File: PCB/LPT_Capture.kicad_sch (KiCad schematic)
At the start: 13 parts, among them J1 USB3155-30-A, J2 DB25P064TXLF, U1 FT245RL

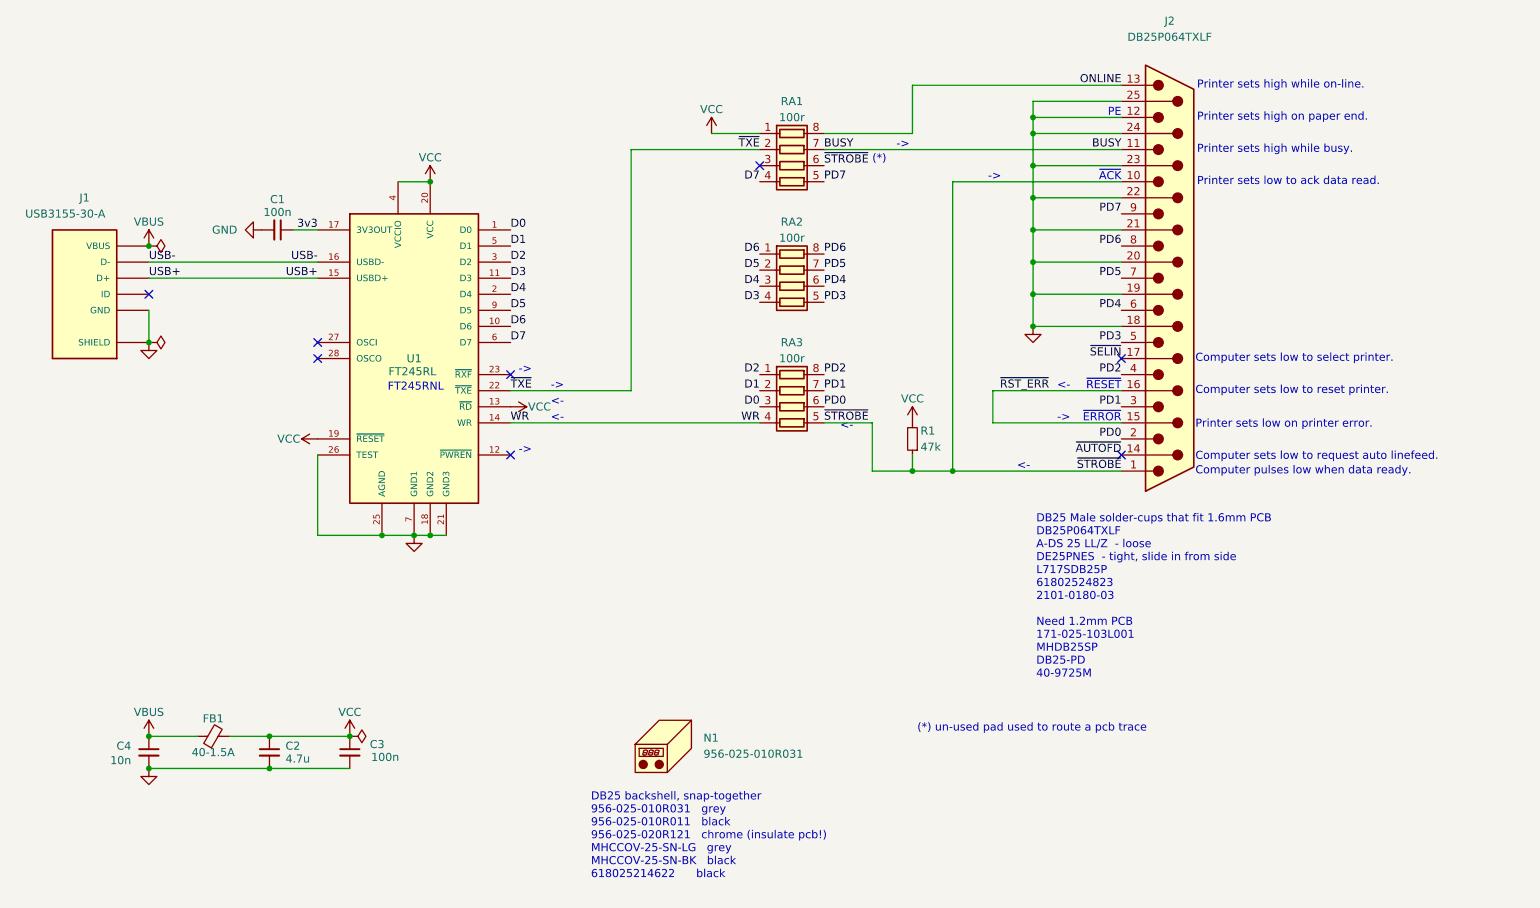
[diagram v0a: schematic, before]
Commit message: strobe>ack via unused 100r
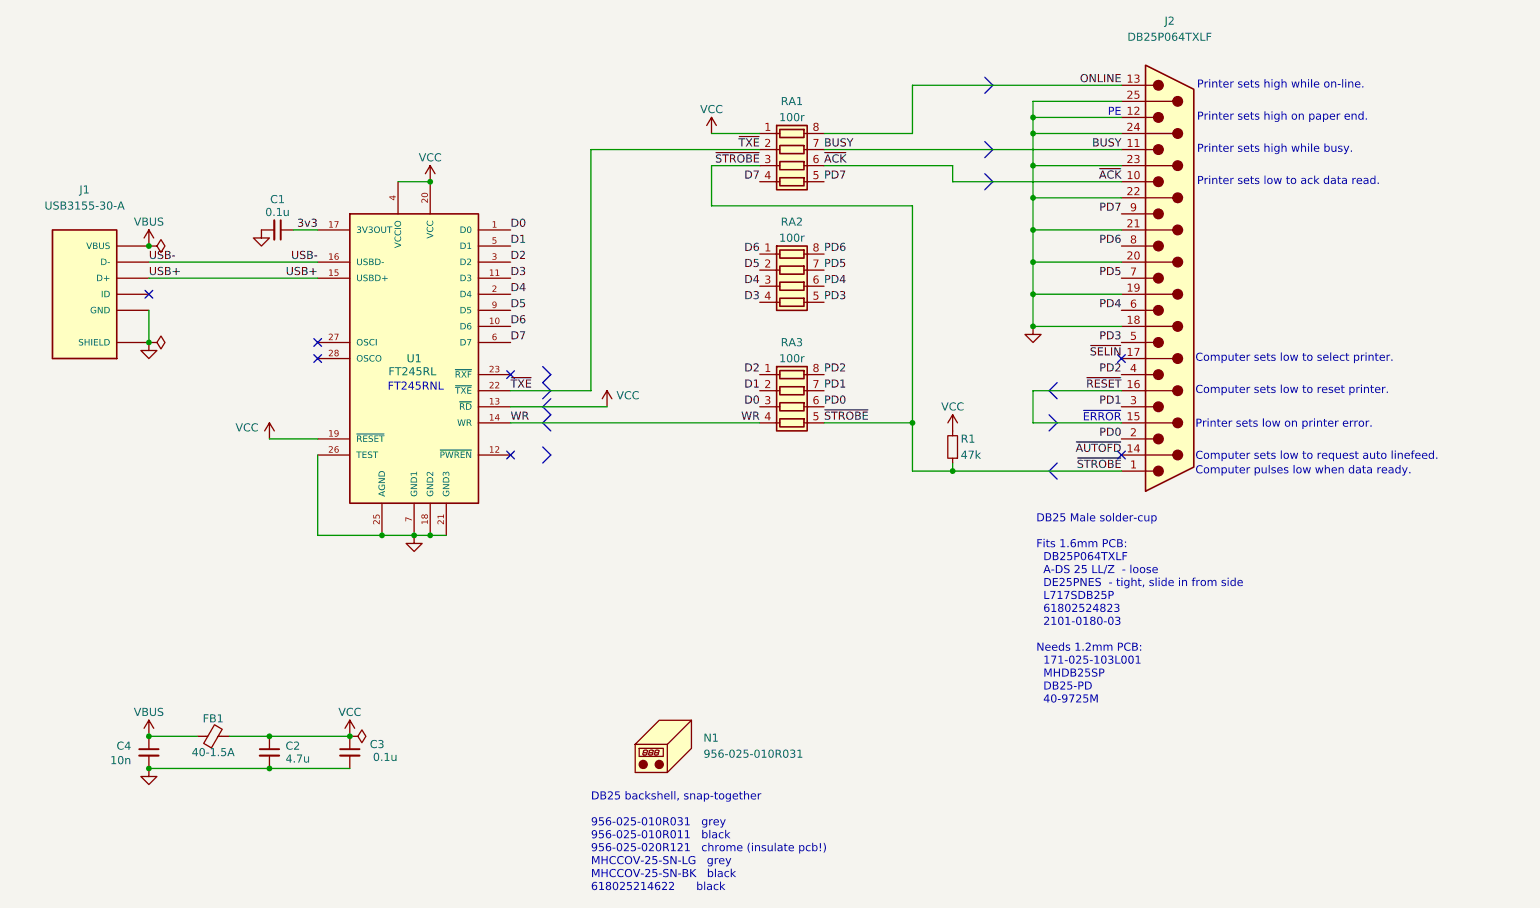
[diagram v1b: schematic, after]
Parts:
- C1, C3: value 100n -> 0.1u
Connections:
- net ~{STROBE}: now also RA1.3 (R3.1); no longer J2.10, RA1.6 (R3.2)
- net ~{RST_ERR} renamed ~{RESET}
- new net ~{ACK}: J2.10, RA1.6 (R3.2)
- no-connect marks 8 -> 7
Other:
- note added: "DB25 Male solder-cup Fits 1.6mm PCB: DB25P064TXLF A-DS 25 LL/Z - loose DE25PNES - tight, slide in from side L717SDB25P 61802524823 2101-0180-03 Needs 1.2mm PCB: 171-025-103L001 MHDB25SP DB25-PD 40-9725M"
- note removed: "(*)"
- note removed: "(*) un-used pad used to route a pcb trace"
- note removed: "->"
- note removed: "<-"
- note removed: "DB25 Male solder-cups that fit 1.6mm PCB DB25P064TXLF A-DS 25 LL/Z - loose DE25PNES - tight, slide in from side L717SDB25P 61802524823 2101-0180-03 Need 1.2mm PCB 171-025-103L001 MHDB25SP DB25-PD 40-9725M"
- note removed: "~{ACK}"
- note removed: "~{RESET}"
- moved on the sheet: R1
